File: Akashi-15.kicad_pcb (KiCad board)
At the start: 2 copper layers, 78.7 x 77.5 mm, 19 parts, among them J1 Conn_02x19_Odd_Even, J2 Conn_02x19_Odd_Even, J3 Conn_01x19_Pin, J4 Conn_01x19_Pin, J5 Conn_01x19_Pin, J6 Conn_01x19_Pin, SW1 SW_Omron_B3FS, SW2 SW_Omron_B3FS

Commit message: Gerber and Schematics generated.
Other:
- board text added: "PC13"
- board text added: "https://github.com/suikan4github/Akashi-15 (C) Seiichi {dblquote}Suikan{dblquote} Horie, 2023"
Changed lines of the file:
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@@
   )
   (setup
+    (stackup
+      (layer "F.SilkS" (type "Top Silk Screen"))
+      (layer "F.Paste" (type "Top Solder Paste"))
+      (layer "F.Mask" (type "Top Solder Mask") (thickness 0.01))
+      (layer "F.Cu" (type "copper") (thickness 0.035))
+      (layer "dielectric 1" (type "core") (thickness 1.51) (material "FR4") (epsilon_r 4.5) (loss_tangent 0.02))
+      (layer "B.Cu" (type "copper") (thickness 0.035))
+      (layer "B.Mask" (type "Bottom Solder Mask") (thickness 0.01))
+      (layer "B.Paste" (type "Bottom Solder Paste"))
+      (layer "B.SilkS" (type "Bottom Silk Screen"))
+      (copper_finish "None")
+      (dielectric_constraints no)
+    )
     (pad_to_mask_clearance 0)
     (pcbplotparams
-      (layerselection 0x00010fc_ffffffff)
+      (layerselection 0x00010f0_ffffffff)
       (plot_on_all_layers_selection 0x0000000_00000000)
       (disableapertmacros false)
       (usegerberextensions false)
-      (usegerberattributes true)
-      (usegerberadvancedattributes true)
+      (usegerberattributes false)
+      (usegerberadvancedattributes false)
       (creategerberjobfile true)
       (dashed_line_dash_ratio 12.000000)
@@
       (outputformat 1)
       (mirror false)
-      (drillshape 1)
+      (drillshape 0)
       (scaleselection 1)
       (outputdirectory "")
@@
   (gr_line (start 193.04 139.7) (end 114.3 139.7)
     (stroke (width 0.1) (type default)) (layer "Edge.Cuts"))
-  (gr_text "Akashi-15" (at 116.84 138.43) (layer "F.SilkS")
+  (gr_text "https://github.com/suikan4github/Akashi-15\n(C) Seiichi {dblquote}Suikan{dblquote} Horie, 2023" (at 170.18 138.43) (layer "B.SilkS")
+    (effects (font (size 1 1) (thickness 0.15)) (justify left bottom mirror))
+  )
+  (gr_text "Akashi-15" (at 147.32 138.43) (layer "F.SilkS")
     (effects (font (size 1.5 1.5) (thickness 0.2)) (justify left bottom))
   )
@@
     (effects (font (size 0.7 0.7) (thickness 0.12) bold) (justify left bottom))
   )
+  (gr_text "PC13" (at 128.27 82.55 90) (layer "F.SilkS")
+    (effects (font (size 1 1) (thickness 0.15)) (justify left bottom))
+  )
   (gr_text "SCL" (at 181.356 91.948 90) (layer "F.SilkS")

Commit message: Forgot to save.
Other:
- board text added: "https://github.com/suikan4github/Akashi-15 (C) Seiichi {dblquote}Suikan{dblquote} Horie, v1.0.0, 2023"
- board text removed: "https://github.com/suikan4github/Akashi-15 (C) Seiichi {dblquote}Suikan{dblquote} Horie, 2023"
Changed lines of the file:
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@@
       (drillshape 0)
       (scaleselection 1)
-      (outputdirectory "")
+      (outputdirectory "gerber/")
     )
   )
@@
   (gr_line (start 193.04 139.7) (end 114.3 139.7)
     (stroke (width 0.1) (type default)) (layer "Edge.Cuts"))
-  (gr_text "https://github.com/suikan4github/Akashi-15\n(C) Seiichi {dblquote}Suikan{dblquote} Horie, 2023" (at 170.18 138.43) (layer "B.SilkS")
+  (gr_text "https://github.com/suikan4github/Akashi-15\n(C) Seiichi {dblquote}Suikan{dblquote} Horie, v1.0.0, 2023" (at 170.18 138.43) (layer "B.SilkS")
     (effects (font (size 1 1) (thickness 0.15)) (justify left bottom mirror))
   )

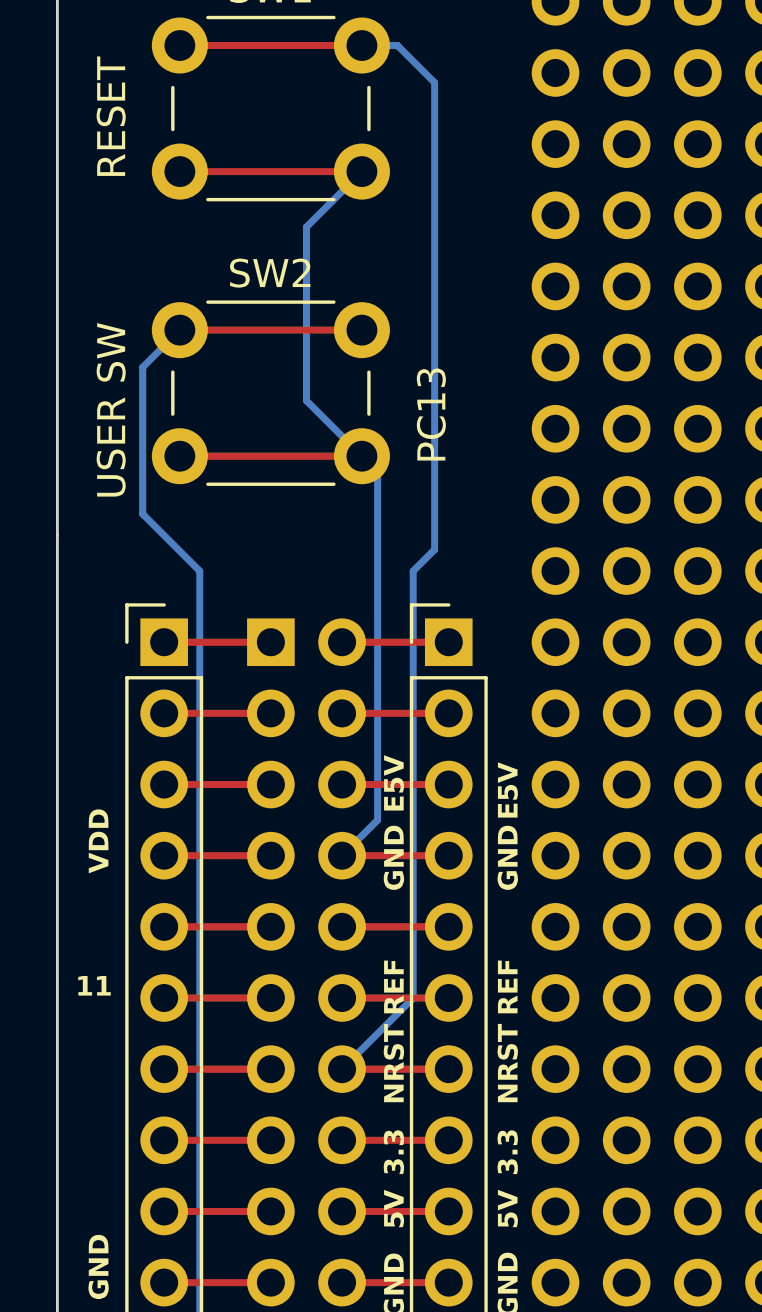
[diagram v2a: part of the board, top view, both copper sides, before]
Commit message: Correct user button connection.
See issue #2 .
https://github.com/suikan4github/Akashi-15/issues/2
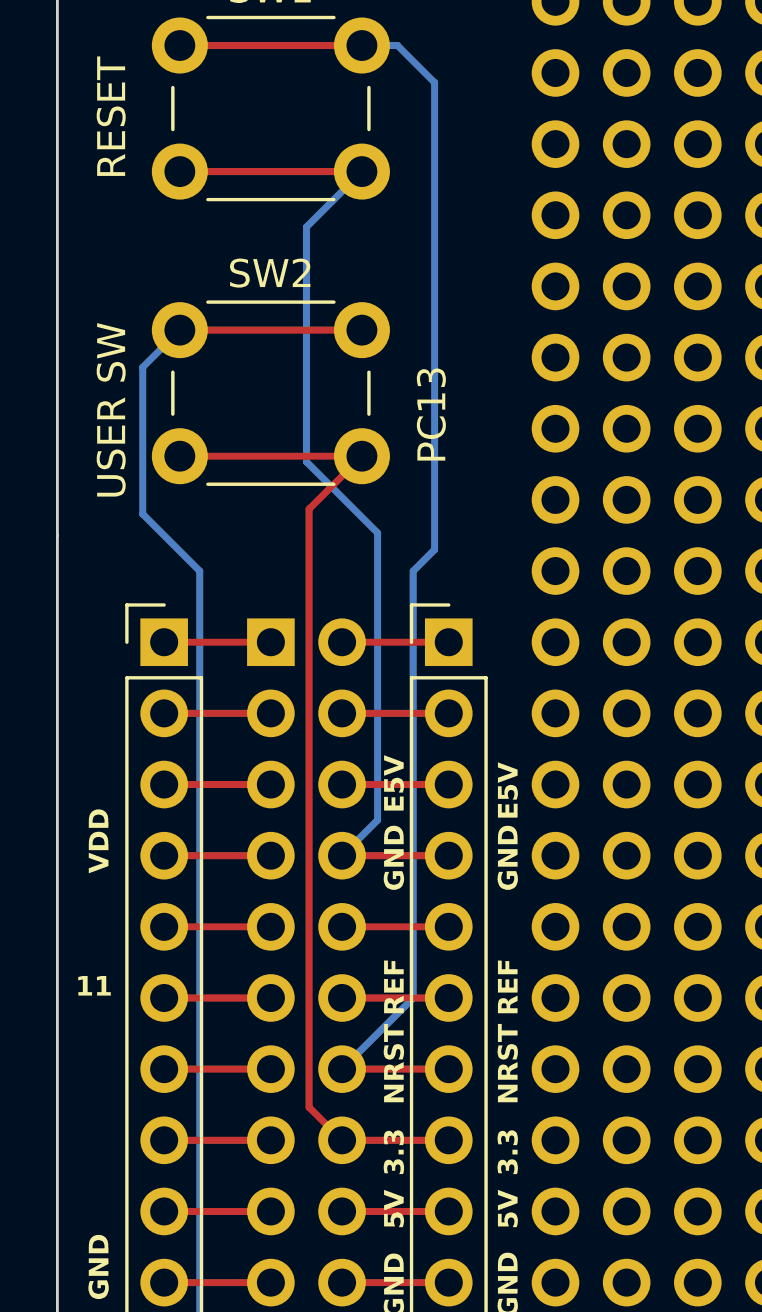
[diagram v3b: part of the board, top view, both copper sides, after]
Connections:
- SW2 pad 2: GND -> Net-(J1-Pin_16)
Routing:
- net Net-(J1-Pin_16): track 3.81 -> 36.0 mm
- net GND: track 43.6 -> 37.1 mm
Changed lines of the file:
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@@
       (net 21 "Net-(J1-Pin_23)") (pinfunction "1") (pintype "passive"))
     (pad "2" thru_hole circle (at 0 4.5 90) (size 2 2) (drill 1.1) (layers "*.Cu" "*.Mask")
-      (net 76 "GND") (pinfunction "2") (pintype "passive"))
+      (net 15 "Net-(J1-Pin_16)") (pinfunction "2") (pintype "passive"))
     (pad "2" thru_hole circle (at 6.5 4.5 90) (size 2 2) (drill 1.1) (layers "*.Cu" "*.Mask")
-      (net 76 "GND") (pinfunction "2") (pintype "passive"))
+      (net 15 "Net-(J1-Pin_16)") (pinfunction "2") (pintype "passive"))
     (model "${KICAD6_3DMODEL_DIR}/Button_Switch_THT.3dshapes/SW_PUSH_6mm.wrl"
       (offset (xyz 0 0 0))
@@
   (segment (start 126.44 67.6) (end 125.17 67.6) (width 0.25) (layer "B.Cu") (net 13))
   (segment (start 121.92 106.68) (end 118.11 106.68) (width 0.25) (layer "F.Cu") (net 14))
+  (segment (start 123.285 84.145) (end 123.285 105.505) (width 0.25) (layer "F.Cu") (net 15))
+  (segment (start 125.17 82.26) (end 123.285 84.145) (width 0.25) (layer "F.Cu") (net 15))
   (segment (start 128.27 106.68) (end 124.46 106.68) (width 0.25) (layer "F.Cu") (net 15))
+  (segment (start 123.285 105.505) (end 124.46 106.68) (width 0.25) (layer "F.Cu") (net 15))
+  (segment (start 118.67 82.26) (end 125.17 82.26) (width 0.25) (layer "F.Cu") (net 15))
   (segment (start 118.11 109.22) (end 121.92 109.22) (width 0.25) (layer "F.Cu") (net 16))
   (segment (start 124.46 109.22) (end 128.27 109.22) (width 0.25) (layer "F.Cu") (net 17))
@@
   (segment (start 128.27 96.52) (end 124.46 96.52) (width 0.25) (layer "F.Cu") (net 76))
   (segment (start 125.17 72.1) (end 118.67 72.1) (width 0.25) (layer "F.Cu") (net 76))
-  (segment (start 118.67 82.26) (end 125.17 82.26) (width 0.25) (layer "F.Cu") (net 76))
-  (segment (start 123.19 74.08) (end 123.19 80.28) (width 0.25) (layer "B.Cu") (net 76))
-  (segment (start 125.73 95.25) (end 124.46 96.52) (width 0.25) (layer "B.Cu") (net 76))
-  (segment (start 125.73 95.25) (end 125.73 82.82) (width 0.25) (layer "B.Cu") (net 76))
-  (segment (start 125.73 82.82) (end 125.17 82.26) (width 0.25) (layer "B.Cu") (net 76))
-  (segment (start 123.19 80.28) (end 125.17 82.26) (width 0.25) (layer "B.Cu") (net 76))
-  (segment (start 125.17 72.1) (end 123.19 74.08) (width 0.25) (layer "B.Cu") (net 76))
+  (segment (start 124.46 96.52) (end 125.73 95.25) (width 0.25) (layer "B.Cu") (net 76))
+  (segment (start 123.19 74.08) (end 125.17 72.1) (width 0.25) (layer "B.Cu") (net 76))
+  (segment (start 125.73 85) (end 123.19 82.46) (width 0.25) (layer "B.Cu") (net 76))
+  (segment (start 123.19 82.46) (end 123.19 74.08) (width 0.25) (layer "B.Cu") (net 76))
+  (segment (start 125.73 95.25) (end 125.73 85) (width 0.25) (layer "B.Cu") (net 76))
   (segment (start 179.07 99.06) (end 182.88 99.06) (width 0.25) (layer "F.Cu") (net 77))
   (segment (start 182.88 83.82) (end 182.88 80.01) (width 0.25) (layer "B.Cu") (net 77))

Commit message: Update version number on sylkscreen.
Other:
- board text added: "https://github.com/suikan4github/Akashi-15 (C) Seiichi {dblquote}Suikan{dblquote} Horie, v1.0.1, 2023"
- board text removed: "https://github.com/suikan4github/Akashi-15 (C) Seiichi {dblquote}Suikan{dblquote} Horie, v1.0.0, 2023"
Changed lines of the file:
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@@
   (gr_line (start 193.04 139.7) (end 114.3 139.7)
     (stroke (width 0.1) (type default)) (layer "Edge.Cuts"))
-  (gr_text "https://github.com/suikan4github/Akashi-15\n(C) Seiichi {dblquote}Suikan{dblquote} Horie, v1.0.0, 2023" (at 170.18 138.43) (layer "B.SilkS")
+  (gr_text "https://github.com/suikan4github/Akashi-15\n(C) Seiichi {dblquote}Suikan{dblquote} Horie, v1.0.1, 2023" (at 170.18 138.43) (layer "B.SilkS")
     (effects (font (size 1 1) (thickness 0.15)) (justify left bottom mirror))
   )
